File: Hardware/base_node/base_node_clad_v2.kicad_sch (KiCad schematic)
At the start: 30 parts, among them J1 IO Interface, J2 RS-422 Connector, J3 Expantion Connector, J4 I2C, J5 Programming Header, J6 Encoder 1, J7 Encoder 2, J8 24vdc, SW1 SW_DIP_x08, U1 CH32X033F8P6, U2 MAX491E, U3 74HC165, U4 MP1584EN_Module

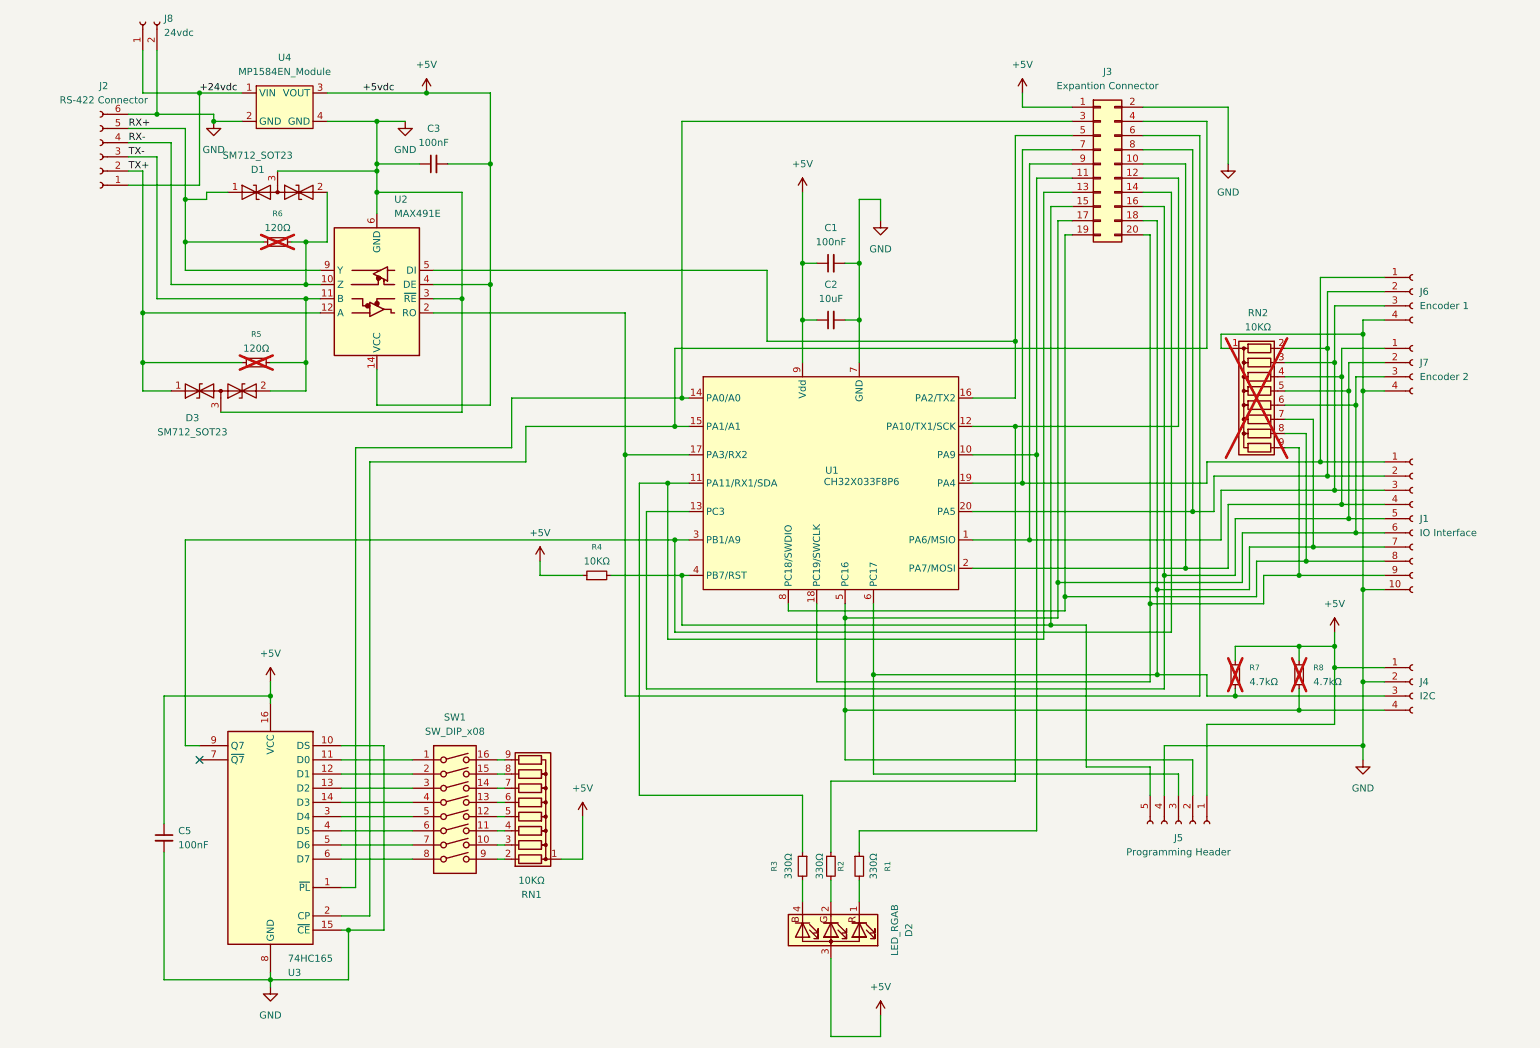
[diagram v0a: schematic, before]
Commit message: docs: establish hierarchical documentation structure and subsystem guides
- Created root navigation hub README.md linking architecture, subsystems, and components
- Added Hardware Subsystem README (bus topology, 24V power rail, RS-422, SM712 protection, BOM)
- Created Base Node README with pinouts (Dev vs Prod), 3D production renders, and manufacturing specs
- Created Gateway Node README with dual-transceiver room segmentation, EEPROM routing, and dev board
- Created Fan Controller Node README with ZCD optocoupler, isolated gate drive, and anti-stall logic
- Created Expanders README with SMD breakout adapter specs and layout previews
- Created Firmware & Protocol Specification README covering 32-bit addressing, packet formats, and dual-slot OTA
- Synchronized KiCad hardware assets, manufacturing plots, and component libraries
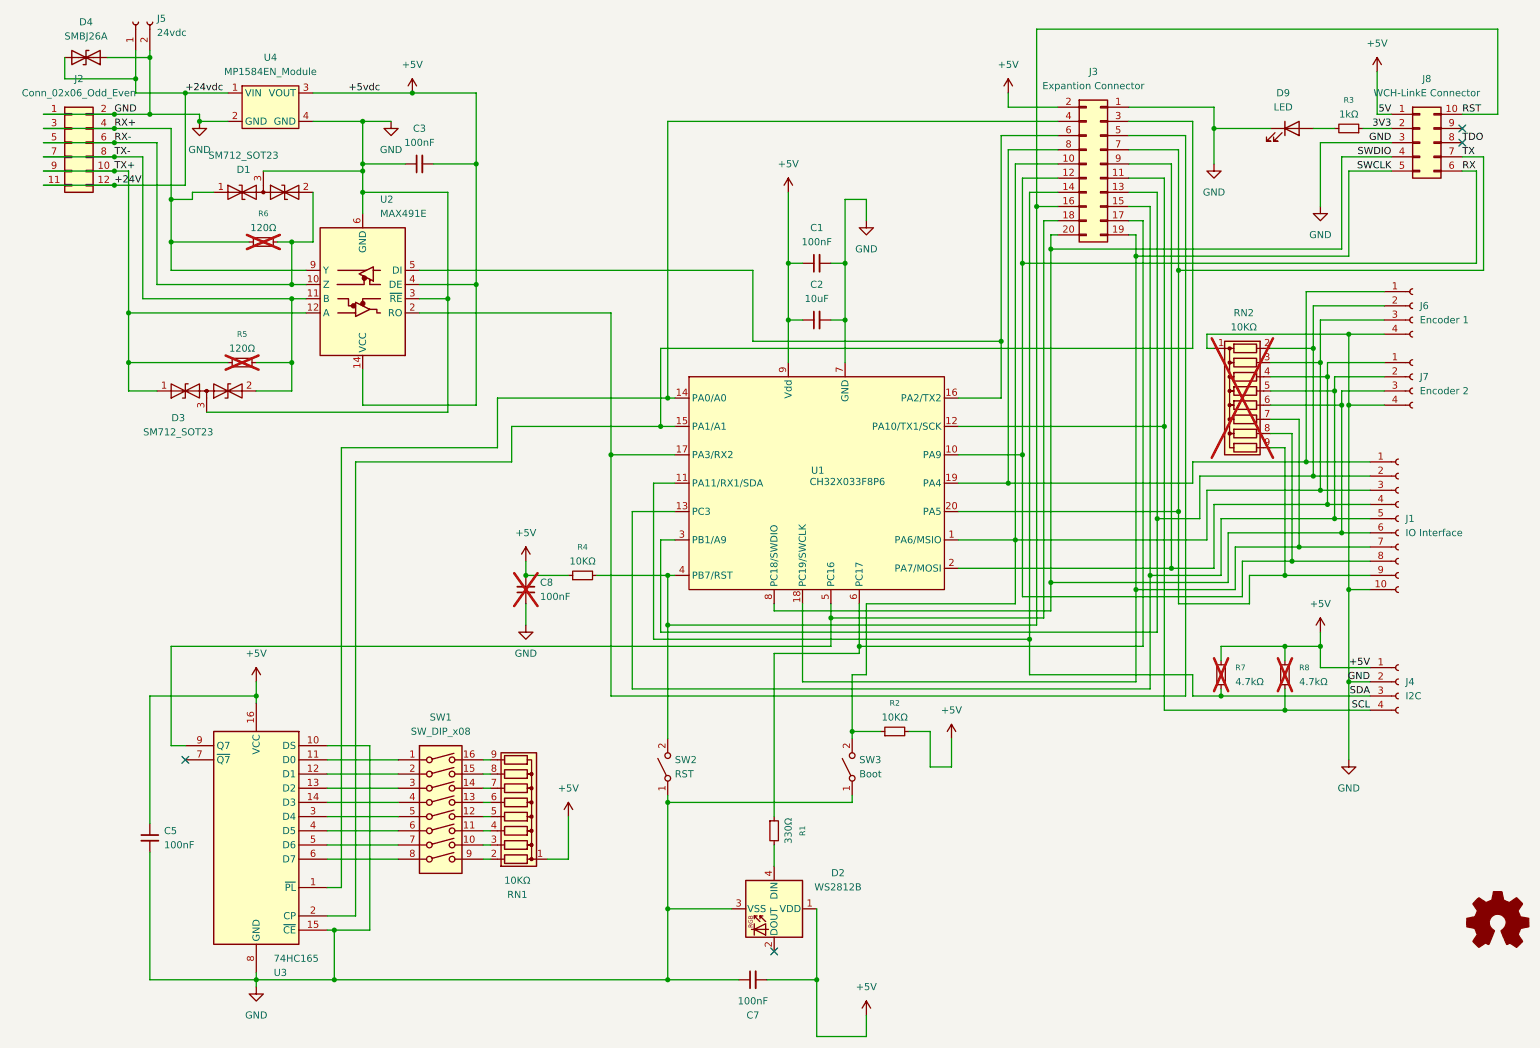
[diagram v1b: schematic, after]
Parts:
- removed D2: LED_RGAB, HomeBus:Crystal_SMD_0603-4Pin_6.0x3.5mm_HandSoldering, symbol HomeBus:LED_RGAB
- removed J2: RS-422 Connector, HomeBus:PhoenixContact_MC_1,5_6-G-5.08_1x06_P5.08mm_Horizontal, symbol Connector:Conn_01x06_Socket
- removed J5: Programming Header, Connector_PinSocket_2.54mm:PinSocket_1x05_P2.54mm_Vertical, symbol Connector:Conn_01x05_Socket
- removed J8: 24vdc, Connector_JST:JST_XH_B2B-XH-A_1x02_P2.50mm_Vertical, symbol Connector:Conn_01x02_Socket
- added C7, C8: 100nF, HomeBus:C_0805_2012Metric_Pad1.18x1.45mm_HandSolder, symbol HomeBus:C_Small
- added D2: WS2812B, LED_SMD:LED_WS2812B_PLCC4_5.0x5.0mm_P3.2mm, symbol HomeBus:WS2812B
- added D4: SMBJ26A, Diode_SMD:D_SMB, symbol Device:D_TVS
- added D9: LED, LED_SMD:LED_1206_3216Metric_Pad1.42x1.75mm_HandSolder, symbol Device:LED
- added J2: Conn_02x06_Odd_Even, Connector_PinSocket_2.54mm:PinSocket_2x06_P2.54mm_Vertical_SMD, symbol Connector_Generic:Conn_02x06_Odd_Even
- added J5: 24vdc, Connector_PinSocket_2.54mm:PinSocket_1x02_P2.54mm_Vertical_SMD_Pin1Left, symbol Connector:Conn_01x02_Socket
- added J8: WCH-LinkE Connector, HomeBus:IDC-Header_2x05_P2.54mm_Vertical_SMD, symbol Connector_Generic:Conn_02x05_Counter_Clockwise
- added SW2: RST, HomeBus:SW_SPST_PTS647_Sx38, symbol Switch:SW_SPST
- added SW3: Boot, HomeBus:SW_SPST_PTS647_Sx38, symbol Switch:SW_SPST
- C1, C2, C3, C5: footprint HomeBus:C_0603_1608Metric -> HomeBus:C_0805_2012Metric_Pad1.18x1.45mm_HandSolder
- J1: footprint HomeBus:JST_PH_B10B-PH-K_1x10_P2.00mm_Vertical -> HomeBus:PinSocket_1x10_P2.54mm_Vertical_SMD_Pin1Left
- J3: footprint HomeBus:IDC-Header_2x10_P2.54mm_Horizontal -> Connector_PinSocket_2.54mm:PinSocket_2x10_P2.54mm_Vertical_SMD
- J4, J6, J7: footprint HomeBus:JST_PH_B4B-PH-K_1x04_P2.00mm_Vertical -> HomeBus:PinSocket_1x04_P2.54mm_Vertical_SMD_Pin1Left
- R1, R4, R5, R6, R7, R8: footprint HomeBus:R_0805_2012Metric -> HomeBus:R_0805_2012Metric_Pad1.20x1.40mm_HandSolder
- R2: value 330Ω -> 10KΩ; footprint HomeBus:R_0805_2012Metric -> HomeBus:R_0805_2012Metric_Pad1.20x1.40mm_HandSolder
- R3: value 330Ω -> 1kΩ; footprint HomeBus:R_0805_2012Metric -> HomeBus:R_0805_2012Metric_Pad1.20x1.40mm_HandSolder
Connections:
- net +5V: now also J3.2 (Pin_1), R2.2, C7.2, C8.2, D2.1 (VDD), J8.1 (Pin_1); no longer J3.1 (Pin_1)
- net GND: now also J3.1 (Pin_2), C7.1, C8.1, D2.3 (VSS), D4.1 (A1), D9.1 (K), J2.1 (Pin_1), J2.2 (Pin_2), J5.2 (Pin_2), J8.3 (Pin_3), SW2.1 (A), SW3.1 (A); no longer J3.2 (Pin_2)
- net RX+: now also J2.3 (Pin_3), J2.4 (Pin_4)
- net RX-: now also J2.5 (Pin_5), J2.6 (Pin_6)
- net TX+: now also J2.10 (Pin_10), J2.9 (Pin_9)
- net TX-: now also J2.7 (Pin_7), J2.8 (Pin_8)
- net RST: now reaches R4.2, U1.4 (PB7/RST)
- net RST: now also J3.16 (Pin_15), J8.10 (Pin_10), SW2.2 (B); no longer J3.15 (Pin_15)
- net at J1.1 (Pin_1), J6.1 (Pin_1), U1.19 (PA4): now also J3.8 (Pin_7); no longer J3.7 (Pin_7)
- net at J1.2 (Pin_2), J6.2 (Pin_2), RN2.2 (R1): now also J3.13 (Pin_14), U1.3 (PB1/A9); no longer J3.8 (Pin_8), U1.20 (PA5)
- net at J1.3 (Pin_3), J6.3 (Pin_3), RN2.3 (R2)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: now also J3.10 (Pin_9), R2.1, SW3.2 (B); no longer J3.9 (Pin_9)
- net at J1.4 (Pin_4), J7.1 (Pin_1), RN2.4 (R3)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: now also J3.9 (Pin_10); no longer J3.10 (Pin_10)
- net at J1.5 (Pin_5), J7.2 (Pin_2), RN2.5 (R4)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: now also J3.15 (Pin_16); no longer J3.16 (Pin_16)
- net RX: now reaches J1.8 (Pin_8), RN2.8 (R7)
- net RX: now also J3.12 (Pin_11), U1.10 (PA9), J8.6 (Pin_6); no longer J3.19 (Pin_19), U1.8 (PC18/SWDIO)
- net TX: now reaches J1.9 (Pin_9), RN2.9 (R8)
- net TX: now also J3.7 (Pin_8), U1.20 (PA5), J8.7 (Pin_7); no longer J3.20 (Pin_20), U1.18 (PC19/SWCLK)
- net at U1.14 (PA0/A0), U3.1 (~{PL}): now also J3.4 (Pin_3); no longer J3.3 (Pin_3)
- net at U1.15 (PA1/A1), U3.2 (CP): now also J3.3 (Pin_4); no longer J3.4 (Pin_4)
- net at U1.16 (PA2/TX2), U2.5 (DI): now also J3.6 (Pin_5); no longer J3.5 (Pin_5)
- net at U1.17 (PA3/RX2), U2.2 (RO): now also J3.5 (Pin_6); no longer J3.6 (Pin_6)
- net at R1.2: now also D2.4 (DIN)
- net at R3.2: now also D9.2 (A)
- net +24vdc renamed +24V
- net +24V: now also D4.2 (A2), J2.11 (Pin_11), J2.12 (Pin_12), J5.1 (Pin_1)
- new net: J3.18 (Pin_17), U1.5 (PC16), U3.9 (Q7)
- new net: J3.17 (Pin_18), R1.1, U1.6 (PC17)
- new net 3V3: J8.2 (Pin_2), R3.1
- new net SCL: J3.11 (Pin_12), J4.4 (Pin_4), R8.2, U1.12 (PA10/TX1/SCK)
- new net SDA: J3.14 (Pin_13), J4.3 (Pin_3), R7.2, U1.11 (PA11/RX1/SDA)
- new net SWCLK: J1.7 (Pin_7), J3.19 (Pin_20), J8.5 (Pin_5), RN2.7 (R6), U1.18 (PC19/SWCLK)
- new net SWDIO: J1.6 (Pin_6), J3.20 (Pin_19), J7.3 (Pin_3), J8.4 (Pin_4), RN2.6 (R5), U1.8 (PC18/SWDIO)
- new net TDO: J8.8 (Pin_8)
- no-connect marks 1 -> 4
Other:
- moved on the sheet: C1, C2, C3, C5, D1, D3, J1, J3, J4, J6, J7, R1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
